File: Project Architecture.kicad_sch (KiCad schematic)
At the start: 0 parts

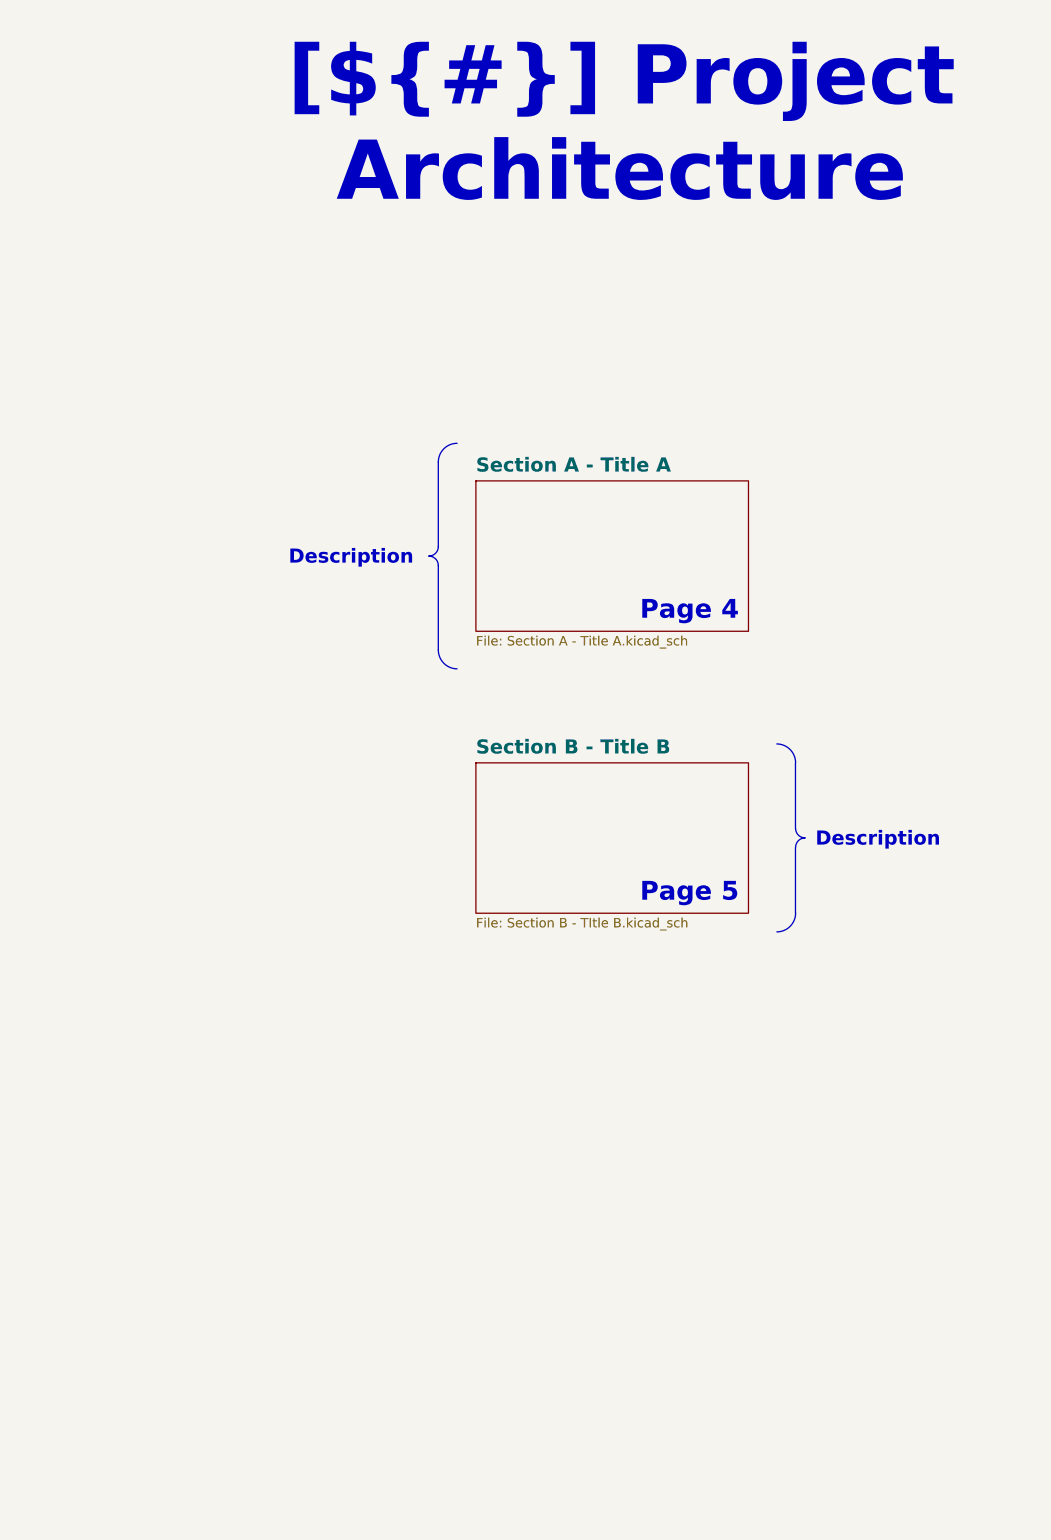
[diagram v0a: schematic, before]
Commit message: Add power supply, connectors, LoRa, gas sensor, audio, and display sheets
Adds nPM1300 power management, USB-C connectors, Minew LoRa module,
multi-gas sensing (CO2/particulate), audio, and display schematics
along with the supporting component libraries and updated PCB routing.

Co-Authored-By: Claude Sonnet 5 <noreply@anthropic.com>
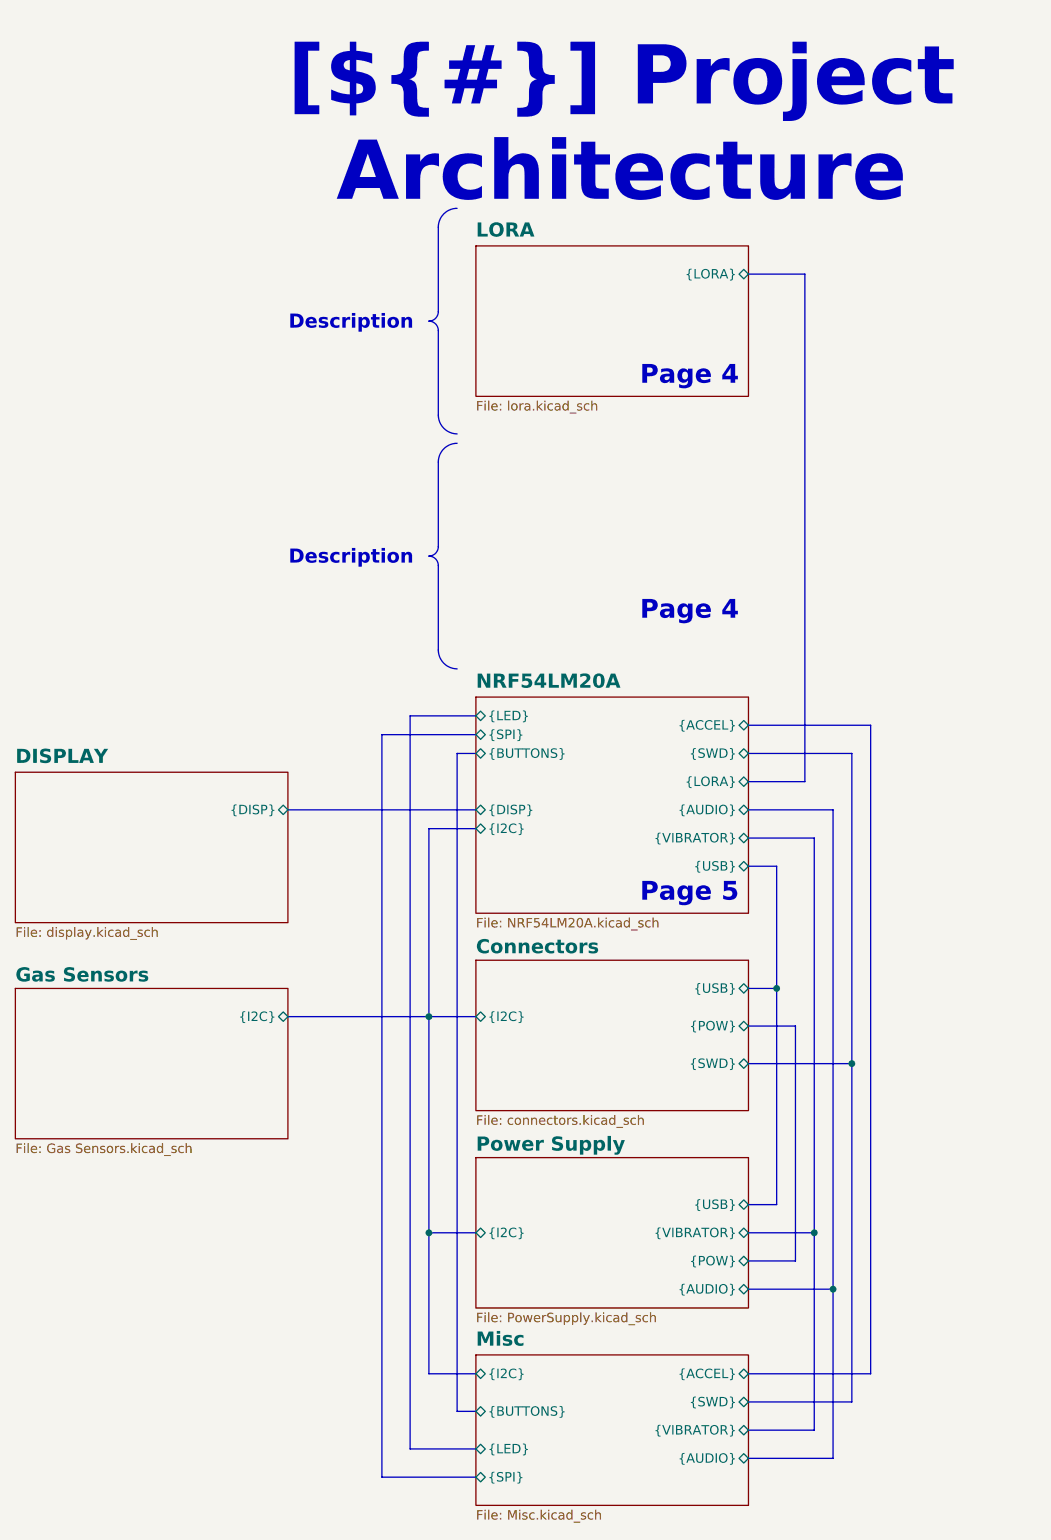
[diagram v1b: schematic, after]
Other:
- sheet Section B - Title B renamed NRF54LM20A
- removed sheet Section A - Title A
- added sheet Connectors (connectors.kicad_sch)
- added sheet DISPLAY (display.kicad_sch)
- added sheet Gas Sensors (Gas Sensors.kicad_sch)
- added sheet LORA (lora.kicad_sch)
- added sheet Misc (Misc.kicad_sch)
- added sheet Power Supply (PowerSupply.kicad_sch)
- sheet NRF54LM20A: file Section B - TItle B.kicad_sch -> NRF54LM20A.kicad_sch
- sheet NRF54LM20A ports: added {ACCEL}, {AUDIO}, {BUTTONS}, {DISP}, {I2C}, {LED}, {LORA}, {SPI}, {SWD}, {USB}, {VIBRATOR}; removed none
